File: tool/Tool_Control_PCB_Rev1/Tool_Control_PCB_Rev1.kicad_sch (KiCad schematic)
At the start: 1 part, among them Q1 MMBT3904

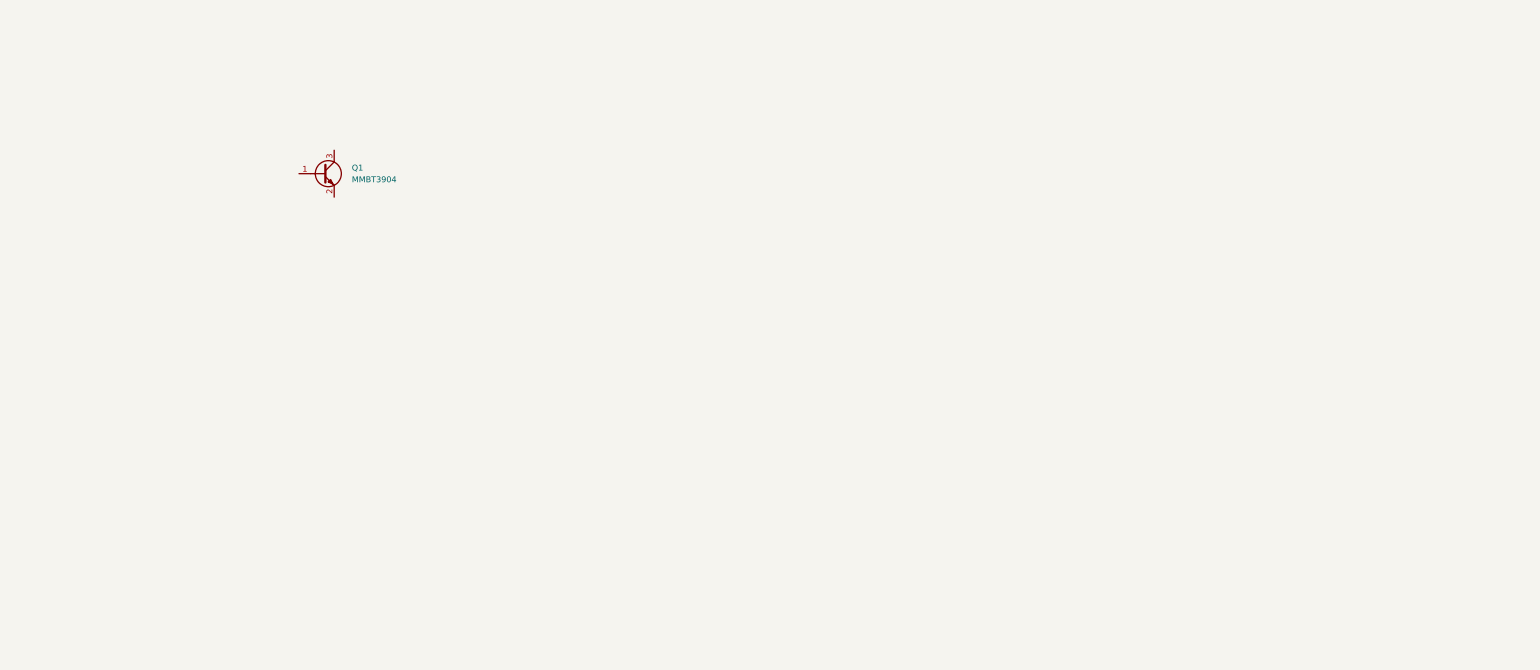
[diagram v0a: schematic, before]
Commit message: worked on pcb for tool control
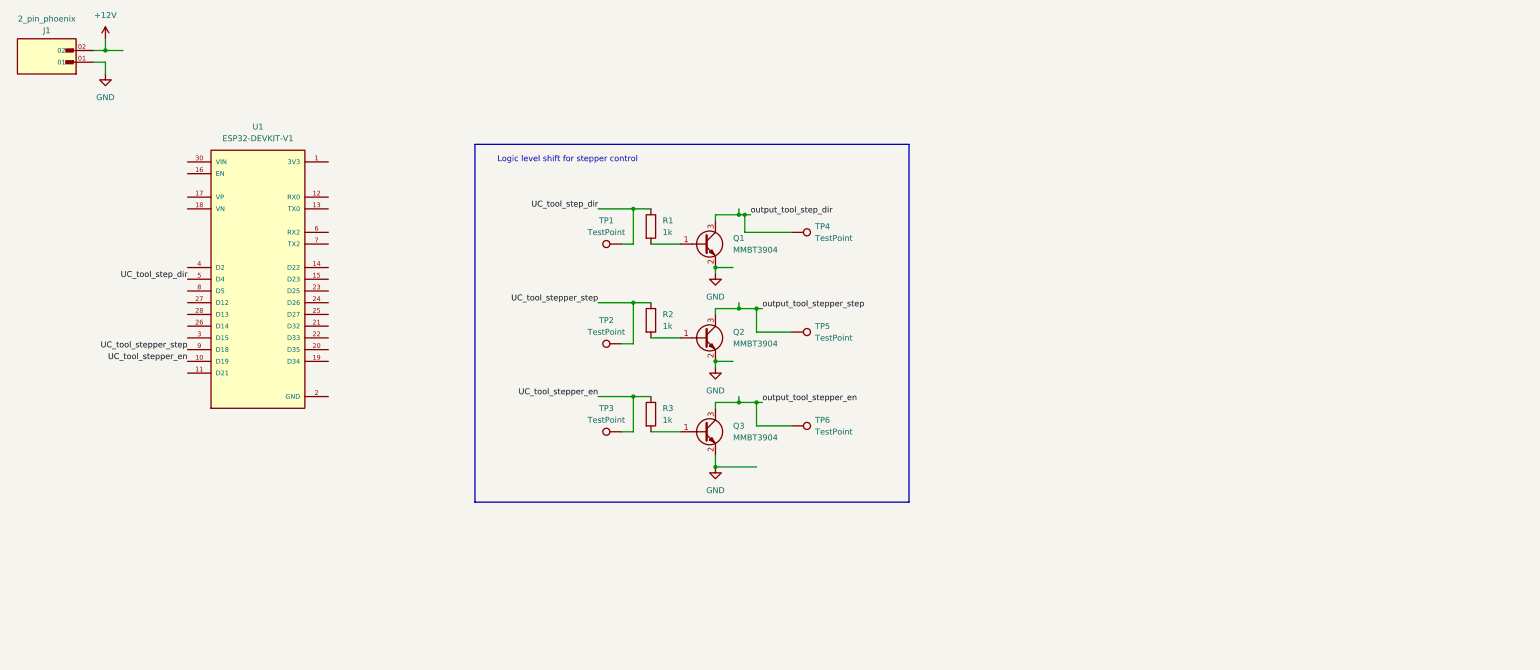
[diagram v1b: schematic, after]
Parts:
- added J1: 2_pin_phoenix, Seed_footprints:PHOENIX_1757242, symbol Seed_syms:2_pin_phoenix
- added Q2, Q3: MMBT3904, Package_TO_SOT_SMD:SOT-23, symbol Transistor_BJT:MMBT3904
- added R1, R2, R3: 1k, Resistor_SMD:R_1206_3216Metric_Pad1.30x1.75mm_HandSolder, symbol Device:R
- added TP1, TP2, TP3, TP4, TP5, TP6: TestPoint, TestPoint:TestPoint_Pad_D3.0mm, symbol Connector:TestPoint
- added U1: ESP32-DEVKIT-V1, Seed_footprints:MODULE_ESP32_DEVKIT_V1, symbol Seed_syms:ESP32-DEVKIT-V1
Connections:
- net at Q1.1 (B): now also R1.2
- net GND: now reaches Q1.2 (E)
- net GND: now also J1.01, Q2.2 (E), Q3.2 (E), U1.2 (GND), U1.29 (GND)
- net output_tool_step_dir: now reaches Q1.3 (C)
- net output_tool_step_dir: now also TP4.1
- new net: Q3.1 (B), R3.2
- new net: Q2.1 (B), R2.2
- new net +12V: J1.02
- new net UC_tool_step_dir: R1.1, TP1.1, U1.5 (D4)
- new net UC_tool_stepper_en: R3.1, TP3.1, U1.10 (D19)
- new net UC_tool_stepper_step: R2.1, TP2.1, U1.9 (D18)
- new net output_tool_stepper_en: Q3.3 (C), TP6.1
- new net output_tool_stepper_step: Q2.3 (C), TP5.1
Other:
- note added: "Logic level shift for stepper control"
- moved on the sheet: Q1

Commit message: PCB work on out of board connections
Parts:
- added J2, J4, J5, J6: Cut Trace/Jumper, symbol Seed_syms:Cut_trace
- added J2: 4_pin_phoenix, CONN_1757268_PXC, symbol Seed_syms:4_pin_phoenix
- added J3, J7: 2_pin_phoenix, Seed_footprints:PHOENIX_1757242, symbol Seed_syms:2_pin_phoenix
- added TP7: TestPoint_2Pole, Seed_footprints:Ground_Point, symbol Connector:TestPoint_2Pole
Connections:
- net +12V: now also J2.1, J3.02
- net GND: now also J3.01, J7.01, TP7.1, TP7.2
- net output_tool_step_dir: now also J5.1
- net output_tool_stepper_en: now also J4.1
- net output_tool_stepper_step: now also J6.1
- net +3.3V: now reaches U1.1 (3V3)
- net +3.3V: now also J2.3
- net TOF_sensor_SDA: now reaches U1.11 (D21)
- net TOF_sensor_SCL: now reaches U1.14 (D22)
- net ALT_tool_stepper_en: now reaches U1.15 (D23)
- net ALT_tool_stepper_en: now also J4.3
- net home_switch: now reaches U1.23 (D25)
- net home_switch: now also J7.02
- net ALT_tool_stepper_step: now reaches U1.6 (D16/RX2)
- net ALT_tool_stepper_step: now also J6.3
- net ALT_tool_stepper_dir: now reaches U1.7 (D17/TX2)
- net ALT_tool_stepper_dir: now also J5.3
- new net Stepper COM+: J2.1, J2.2
- new net Stepper Dir: J2.3, J5.2
- new net Stepper EN: J2.4, J4.2
- new net Stepper Step: J2.2, J6.2
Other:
- note added: "Driver"
- note added: "Home Switch Connection"
- note added: "TOF Sensor Connection"
- moved on the sheet: Q1, Q2, Q3, R1, R2, R3, TP1, TP2, TP3, TP4, TP5, TP6
